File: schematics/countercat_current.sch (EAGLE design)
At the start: 59 parts, among them Q1 IRF520, Q3 IRF520, Q4 IRF520, Q5 IRF520, U4 ATMEGA328P, Y1 16MHz

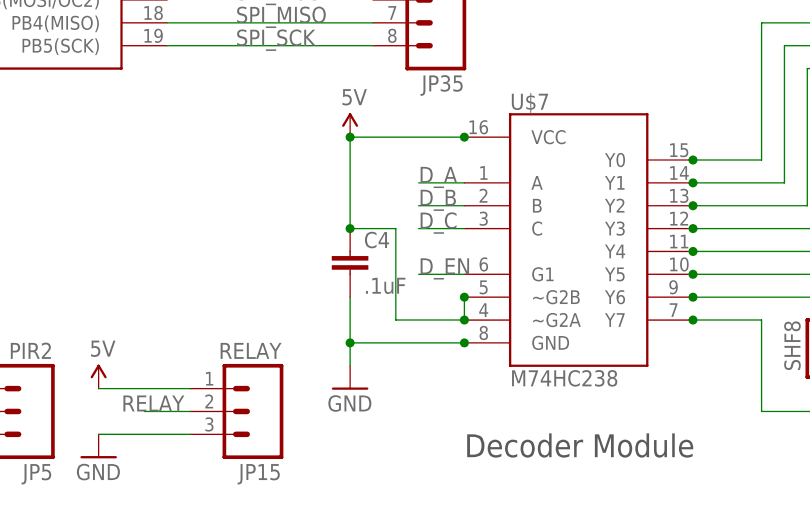
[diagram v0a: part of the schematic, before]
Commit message: Updated current schematic file to fix mistakes from Rev3 board.
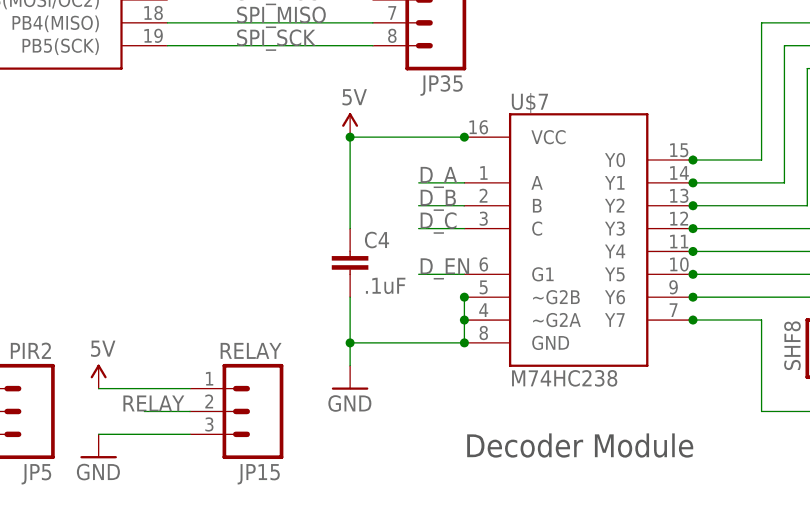
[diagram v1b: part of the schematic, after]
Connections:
- removed net N$8: C3.1, U4.AREF, U4.AVCC, U4.VCC
- net 5V: now also C3.1, U4.AREF, U4.AVCC, U4.VCC; no longer U$7.~G2A, U$7.~G2B
- net GND: now also U$7.~G2A, U$7.~G2B
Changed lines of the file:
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@@
 <wire x1="22.86" y1="5.08" x2="22.86" y2="-5.08" width="0.1524" layer="91"/>
 <pinref part="C4" gate="G$1" pin="1"/>
-<junction x="22.86" y="-5.08"/>
 <junction x="22.86" y="5.08"/>
-<pinref part="U$7" gate="G$1" pin="~G2B"/>
-<pinref part="U$7" gate="G$1" pin="~G2A"/>
-<wire x1="35.56" y1="-12.7" x2="35.56" y2="-15.24" width="0.1524" layer="91"/>
-<wire x1="35.56" y1="-15.24" x2="27.94" y2="-15.24" width="0.1524" layer="91"/>
-<wire x1="27.94" y1="-15.24" x2="27.94" y2="-5.08" width="0.1524" layer="91"/>
-<wire x1="27.94" y1="-5.08" x2="22.86" y2="-5.08" width="0.1524" layer="91"/>
-<junction x="35.56" y="-15.24"/>
-<junction x="35.56" y="-12.7"/>
 <junction x="35.56" y="5.08"/>
 </segment>
@@
 <pinref part="U$1" gate="G$1" pin="5V"/>
 <wire x1="-5.08" y1="-22.86" x2="5.08" y2="-22.86" width="0.1524" layer="91"/>
+</segment>
+<segment>
+<wire x1="-45.72" y1="66.04" x2="-63.5" y2="66.04" width="0.1524" layer="91"/>
+<pinref part="U4" gate="G$1" pin="VCC"/>
+<pinref part="U4" gate="G$1" pin="AVCC"/>
+<wire x1="-45.72" y1="68.58" x2="-45.72" y2="66.04" width="0.1524" layer="91"/>
+<junction x="-45.72" y="66.04"/>
+<pinref part="U4" gate="G$1" pin="AREF"/>
+<wire x1="-45.72" y1="58.42" x2="-45.72" y2="66.04" width="0.1524" layer="91"/>
+<wire x1="-63.5" y1="63.5" x2="-63.5" y2="66.04" width="0.1524" layer="91"/>
+<pinref part="C3" gate="G$1" pin="1"/>
+<junction x="-63.5" y="66.04"/>
+<wire x1="-63.5" y1="66.04" x2="-63.5" y2="68.58" width="0.1524" layer="91"/>
+<pinref part="U$6" gate="G$1" pin="5V"/>
 </segment>
 </net>
@@
 <junction x="22.86" y="-17.78"/>
 <junction x="35.56" y="-17.78"/>
+<pinref part="U$7" gate="G$1" pin="~G2A"/>
+<pinref part="U$7" gate="G$1" pin="~G2B"/>
+<junction x="35.56" y="-12.7"/>
+<wire x1="35.56" y1="-12.7" x2="35.56" y2="-15.24" width="0.1524" layer="91"/>
+<junction x="35.56" y="-15.24"/>
+<wire x1="35.56" y1="-15.24" x2="35.56" y2="-17.78" width="0.1524" layer="91"/>
 </segment>
 <segment>
@@
 </segment>
 </net>
-<net name="N$8" class="0">
-<segment>
-<wire x1="-45.72" y1="66.04" x2="-63.5" y2="66.04" width="0.1524" layer="91"/>
-<pinref part="U4" gate="G$1" pin="VCC"/>
-<pinref part="U4" gate="G$1" pin="AVCC"/>
-<wire x1="-45.72" y1="68.58" x2="-45.72" y2="66.04" width="0.1524" layer="91"/>
-<junction x="-45.72" y="66.04"/>
-<pinref part="U4" gate="G$1" pin="AREF"/>
-<wire x1="-45.72" y1="58.42" x2="-45.72" y2="66.04" width="0.1524" layer="91"/>
-<wire x1="-63.5" y1="63.5" x2="-63.5" y2="66.04" width="0.1524" layer="91"/>
-<pinref part="C3" gate="G$1" pin="1"/>
-<junction x="-63.5" y="66.04"/>
-<wire x1="-63.5" y1="66.04" x2="-63.5" y2="68.58" width="0.1524" layer="91"/>
-</segment>
-</net>
